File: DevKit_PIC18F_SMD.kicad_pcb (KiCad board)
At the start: 2 copper layers, 27 x 53.5 mm, 25 parts, among them J1 PIC_ICSP_ICD, J2 USB_B_Mini, J5 RIGHT_PORT, J6 LEFT_PORT, SW1 SW_RST, X1 16MHz

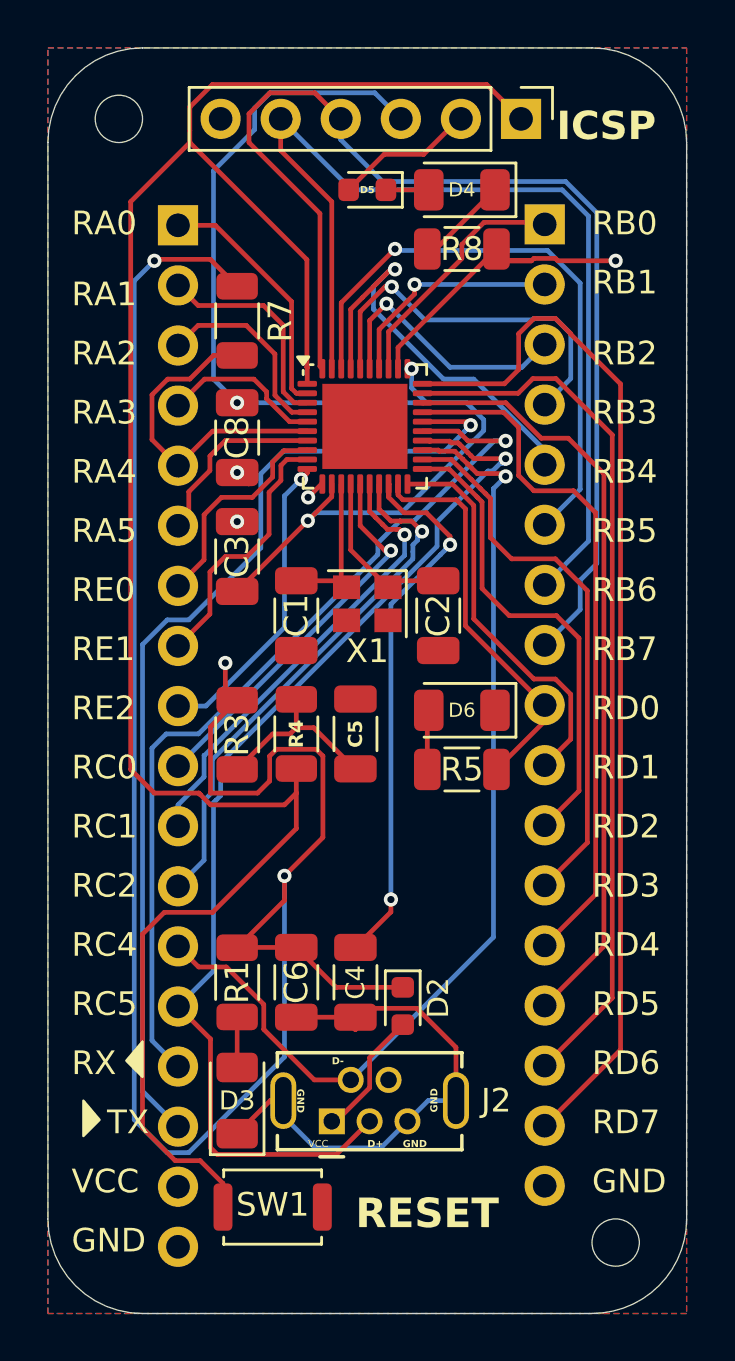
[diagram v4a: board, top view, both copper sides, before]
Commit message: Rev.3 : refine part-selection for JLCPCB fabrication & silkscreen.
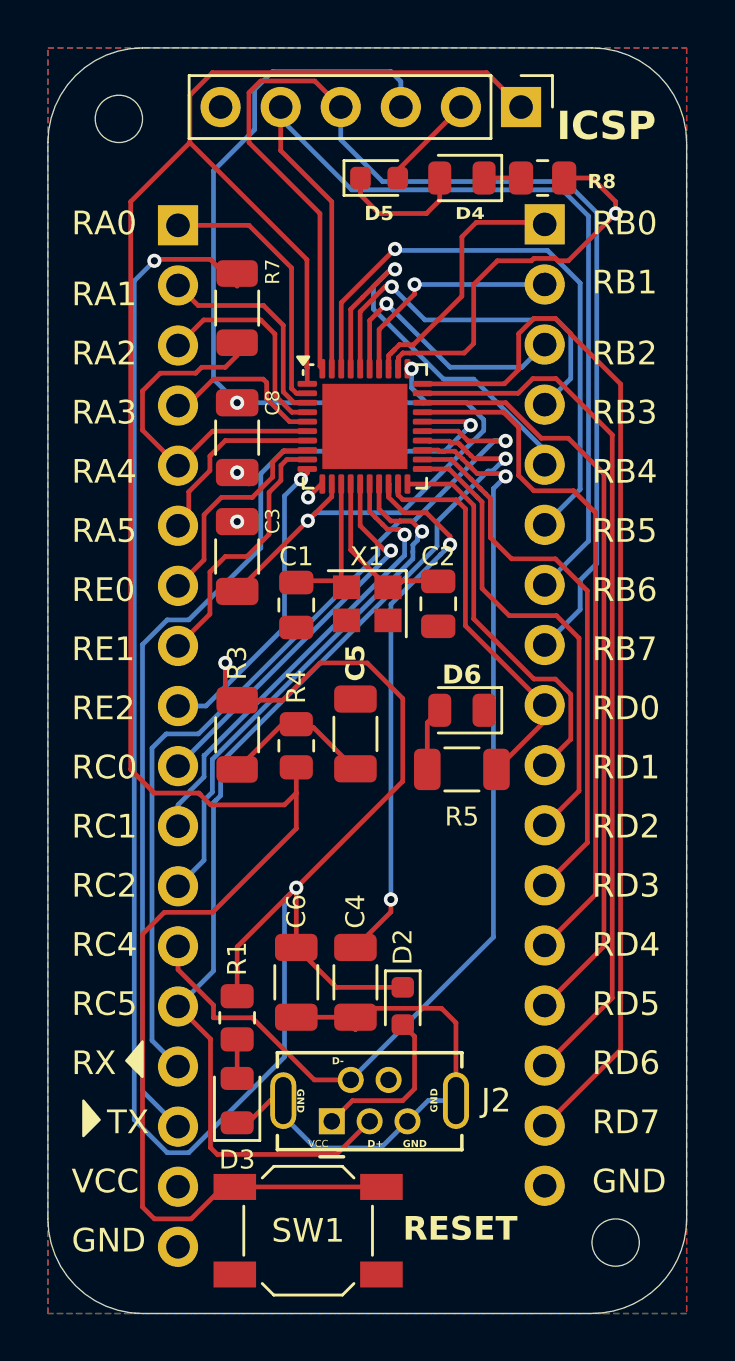
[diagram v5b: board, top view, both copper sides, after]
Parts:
- C1, C2: footprint Capacitor_SMD:C_1206_3216Metric -> Capacitor_SMD:C_0805_2012Metric
- D3, D4, D6: footprint LED_SMD:LED_1206_3216Metric -> LED_SMD:LED_0805_2012Metric
- PIC18F45K50: value PIC18F45K50-I/P -> PIC18F45K50-I/MV
- R1, R8: value 330 -> 470; footprint Resistor_SMD:R_1206_3216Metric -> Resistor_SMD:R_0805_2012Metric
- R4: footprint Resistor_SMD:R_1206_3216Metric -> Resistor_SMD:R_0805_2012Metric
- R5: value 330 -> 470
- SW1: value SW_RST -> C318938; footprint Button_Switch_SMD:SW_Push_SPST_NO_Alps_SKRK -> Button_Switch_SMD:SW_SPST_SKQG_WithStem
- moved R8 4.54 mm to (92.9, 32.0)
- moved SW1 1.80 mm to (83.0, 76.5)
- moved R1 1.50 mm to (80.0, 67.5)
- moved D5 0.71 mm to (86.0, 32.0), turned to 0 degrees
- moved R7 0.54 mm to (80.0, 37.5)
- moved C2 0.50 mm to (88.5, 50.0)
- moved D4 0.50 mm to (89.5, 32.0)
- moved J1 0.50 mm to (92.0, 29.0)
- moved R4 0.50 mm to (82.5, 56.0)
- moved C1 0.45 mm to (82.5, 50.0)
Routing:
- net /MCLR: track 88.7 -> 98.0 mm
- net VCC: track 101.6 -> 108.2 mm
- net Net-(D4-A): track 1.81 -> 5.56 mm
- net Net-(D4-K): track 3.90 -> 1.56 mm
- net Net-(D2-A): track 5.44 -> 7.17 mm
- net GND: track 71.8 -> 73.2 mm
- net Net-(D5-A): track 5.99 -> 4.61 mm
- net /RA4: track 13.8 -> 15.0 mm
- net Net-(J5-Pin_1): track 10.9 -> 11.9 mm
- net Net-(C5-Pad2): track 8.18 -> 7.11 mm
- net /RA0: track 10.6 -> 11.4 mm
- net /PGD: track 48.9 -> 49.7 mm
- net /RA2: track 8.35 -> 9.04 mm
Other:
- board text added: "DevKit_SMD PIC18F45K50 Rev.3 : 8th March, 2025 Designed by @deulamco"
- board text removed: "DevKit_SMD PIC18F45K50 Rev.2 : 7th March, 2025 Designed by @deulamco"

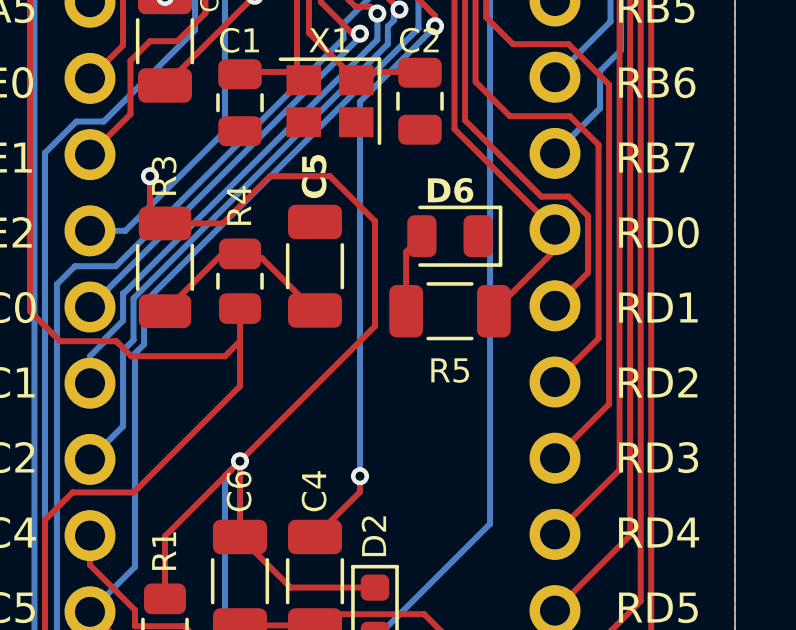
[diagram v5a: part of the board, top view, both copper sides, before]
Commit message: :Fix R5 size 1206 -> 0805 & BOM of D5,D2 -> C3758192
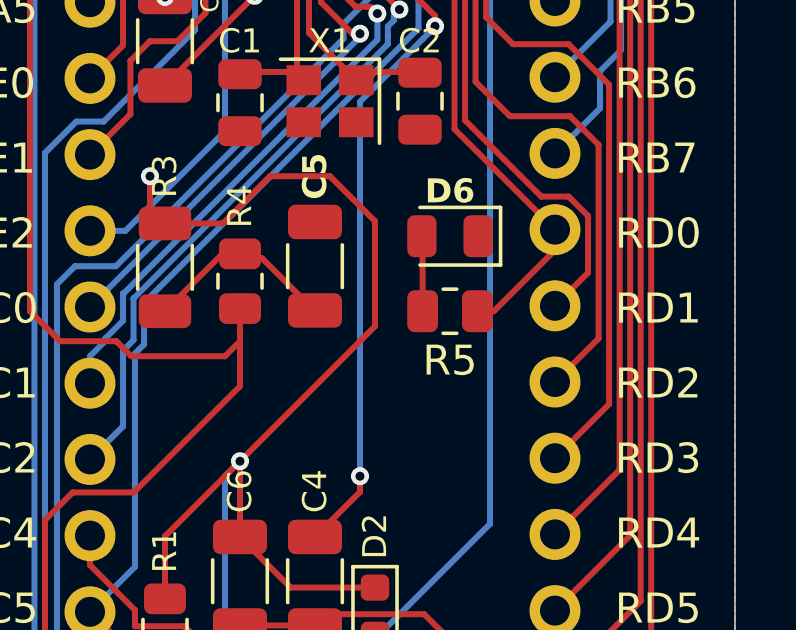
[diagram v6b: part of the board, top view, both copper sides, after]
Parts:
- R5: footprint Resistor_SMD:R_1206_3216Metric -> Resistor_SMD:R_0805_2012Metric
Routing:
- net Net-(D6-A): track 2.72 -> 1.96 mm
- net /RD0: track 16.8 -> 17.3 mm
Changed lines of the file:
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@@
 		)
 	)
-	(footprint "Resistor_SMD:R_1206_3216Metric"
+	(footprint "Resistor_SMD:R_0805_2012Metric"
 		(layer "F.Cu")
 		(at 89.5 57 180)
-		(descr "Resistor SMD 1206 (3216 Metric), square (rectangular) end terminal, IPC_7351 nominal, (Body size source: IPC-SM-782 page 72, https://www.pcb-3d.com/wordpress/wp-content/uploads/ipc-sm-782a_amendment_1_and_2.pdf), generated with kicad-footprint-generator")
+		(descr "Resistor SMD 0805 (2012 Metric), square (rectangular) end terminal, IPC_7351 nominal, (Body size source: IPC-SM-782 page 72, https://www.pcb-3d.com/wordpress/wp-content/uploads/ipc-sm-782a_amendment_1_and_2.pdf), generated with kicad-footprint-generator")
 		(tags "resistor")
 		(property "Reference" "R5"
-			(at 0 -2 0)
+			(at 0 -1.65 180)
 			(layer "F.SilkS")
 			(effects
 				(font
-					(size 0.8 0.8)
-					(thickness 0.125)
+					(size 1 1)
+					(thickness 0.15)
 				)
 			)
 		)
 		(property "Value" "470"
-			(at 0 1.82 0)
+			(at 0 1.65 180)
 			(layer "F.Fab")
 			(effects
@@
 		(attr smd)
 		(fp_line
-			(start -0.727064 0.91)
-			(end 0.727064 0.91)
+			(start -0.227064 0.735)
+			(end 0.227064 0.735)
 			(stroke
 				(width 0.12)
@@
 		)
 		(fp_line
-			(start -0.727064 -0.91)
-			(end 0.727064 -0.91)
+			(start -0.227064 -0.735)
+			(end 0.227064 -0.735)
 			(stroke
 				(width 0.12)
@@
 		)
 		(fp_line
-			(start 2.28 1.12)
-			(end -2.28 1.12)
+			(start 1.68 0.95)
+			(end -1.68 0.95)
 			(stroke
 				(width 0.05)
@@
 		)
 		(fp_line
-			(start 2.28 -1.12)
-			(end 2.28 1.12)
+			(start 1.68 -0.95)
+			(end 1.68 0.95)
 			(stroke
 				(width 0.05)
@@
 		)
 		(fp_line
-			(start -2.28 1.12)
-			(end -2.28 -1.12)
+			(start -1.68 0.95)
+			(end -1.68 -0.95)
 			(stroke
 				(width 0.05)
@@
 		)
 		(fp_line
-			(start -2.28 -1.12)
-			(end 2.28 -1.12)
+			(start -1.68 -0.95)
+			(end 1.68 -0.95)
 			(stroke
 				(width 0.05)
@@
 		)
 		(fp_line
-			(start 1.6 0.8)
-			(end -1.6 0.8)
+			(start 1 0.625)
+			(end -1 0.625)
 			(stroke
 				(width 0.1)
@@
 		)
 		(fp_line
-			(start 1.6 -0.8)
-			(end 1.6 0.8)
+			(start 1 -0.625)
+			(end 1 0.625)
 			(stroke
 				(width 0.1)
@@
 		)
 		(fp_line
-			(start -1.6 0.8)
-			(end -1.6 -0.8)
+			(start -1 0.625)
+			(end -1 -0.625)
 			(stroke
 				(width 0.1)
@@
 		)
 		(fp_line
-			(start -1.6 -0.8)
-			(end 1.6 -0.8)
+			(start -1 -0.625)
+			(end 1 -0.625)
 			(stroke
 				(width 0.1)
@@
 		)
 		(fp_text user "${REFERENCE}"
-			(at 0 0 0)
+			(at 0 0 180)
 			(layer "F.Fab")
 			(effects
 				(font
-					(size 0.8 0.8)
-					(thickness 0.12)
+					(size 0.5 0.5)
+					(thickness 0.08)
 				)
 			)
 		)
 		(pad "1" smd roundrect
-			(at -1.4625 0 180)
-			(size 1.125 1.75)
+			(at -0.9125 0 180)
+			(size 1.025 1.4)
 			(layers "F.Cu" "F.Mask" "F.Paste")
-			(roundrect_rratio 0.222222)
+			(roundrect_rratio 0.243902)
 			(net 47 "/RD0")
 			(pintype "passive")
 		)
 		(pad "2" smd roundrect
-			(at 1.4625 0 180)
-			(size 1.125 1.75)
+			(at 0.9125 0 180)
+			(size 1.025 1.4)
 			(layers "F.Cu" "F.Mask" "F.Paste")
-			(roundrect_rratio 0.222222)
+			(roundrect_rratio 0.243902)
 			(net 26 "Net-(D6-A)")
 			(pintype "passive")
 		)
 		(embedded_fonts no)
-		(model "${KICAD9_3DMODEL_DIR}/Resistor_SMD.3dshapes/R_1206_3216Metric.wrl"
+		(model "${KICAD9_3DMODEL_DIR}/Resistor_SMD.3dshapes/R_0805_2012Metric.wrl"
 			(offset
 				(xyz 0 0 0)
@@
 	)
 	(segment
-		(start 88.0375 55.025)
-		(end 88.0375 57)
+		(start 88.5875 54.525)
+		(end 88.5875 56.45)
 		(width 0.2)
 		(layer "F.Cu")
@@
 	(segment
 		(start 88.5625 54.5)
-		(end 88.0375 55.025)
+		(end 88.5875 54.525)
 		(width 0.2)
 		(layer "F.Cu")
@@
 	)
 	(segment
-		(start 93 54.9625)
-		(end 93 54.28)
+		(start 89.651 45.985552)
+		(end 89.266448 45.601)
 		(width 0.2)
 		(layer "F.Cu")
@@
 	)
 	(segment
-		(start 89.651 45.985552)
-		(end 89.266448 45.601)
+		(start 86.8 45.395088)
+		(end 86.8 44.9375)
 		(width 0.2)
 		(layer "F.Cu")
@@
 	)
 	(segment
-		(start 86.8 45.395088)
-		(end 86.8 44.9375)
+		(start 93 54.9625)
+		(end 93 54.28)
 		(width 0.2)
 		(layer "F.Cu")
@@
 		(width 0.2)
 		(layer "F.Cu")
+		(net 47)
+	)
+	(segment
+		(start 90.4125 57)
+		(end 90.9625 57)
+		(width 0.2)
+		(layer "F.Cu")
